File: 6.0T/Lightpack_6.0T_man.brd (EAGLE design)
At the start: 78 x 78.1 mm, 31 parts, among them CN1 USB-MICRO-B-EVT, CN2 RJ11-5P-REEL-LIGHTPACK6T2, CN3 RJ11-5P-REEL-MAIN, IC1 AT90USB162, IC2 DM631_SOP24, IC3 DM631_SOP24, J1 DCJ0202, X1 16Mhz

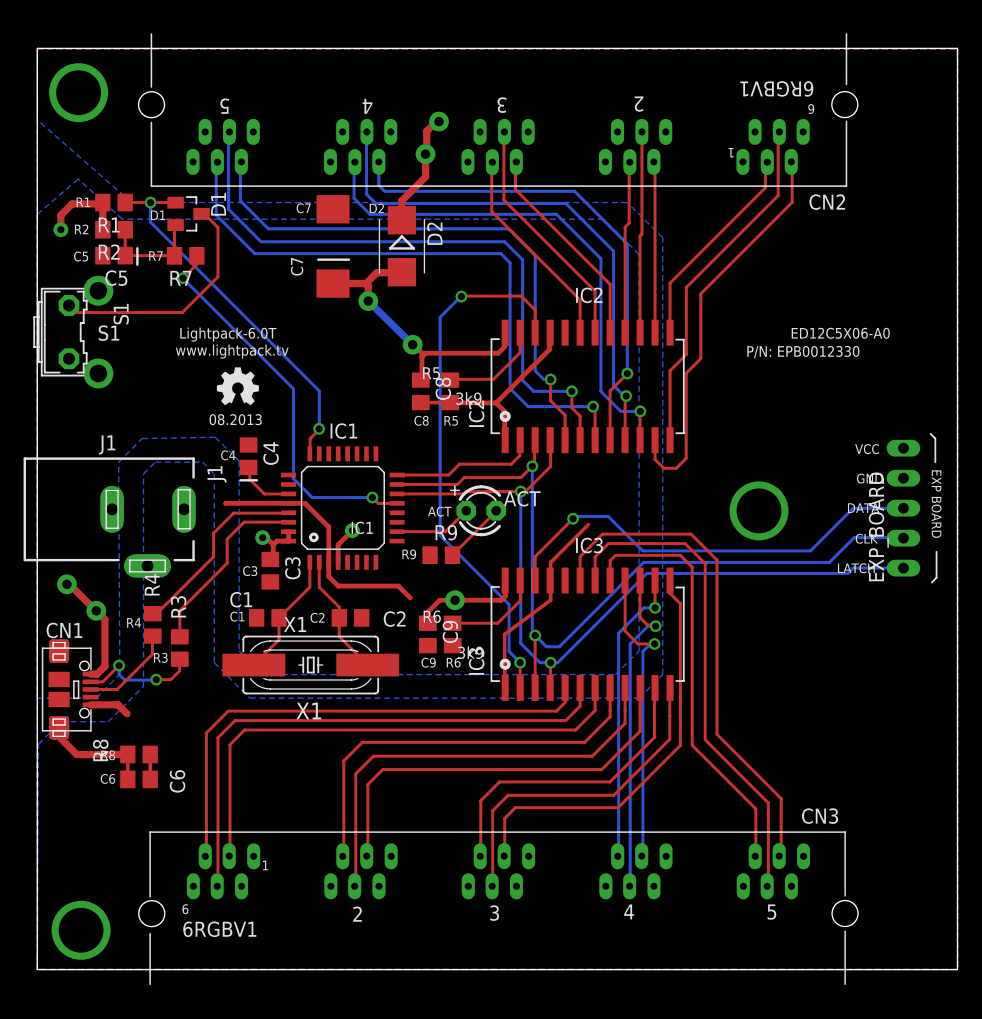
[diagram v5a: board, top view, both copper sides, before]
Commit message: LED, RJ11 reel, Soldermask
— Indicator LED shifted to the exp board on 1.3 mm
— RJ11 reel pads with increased drill diameter
— All vias up to 0.6 diameters now covers with soldermask
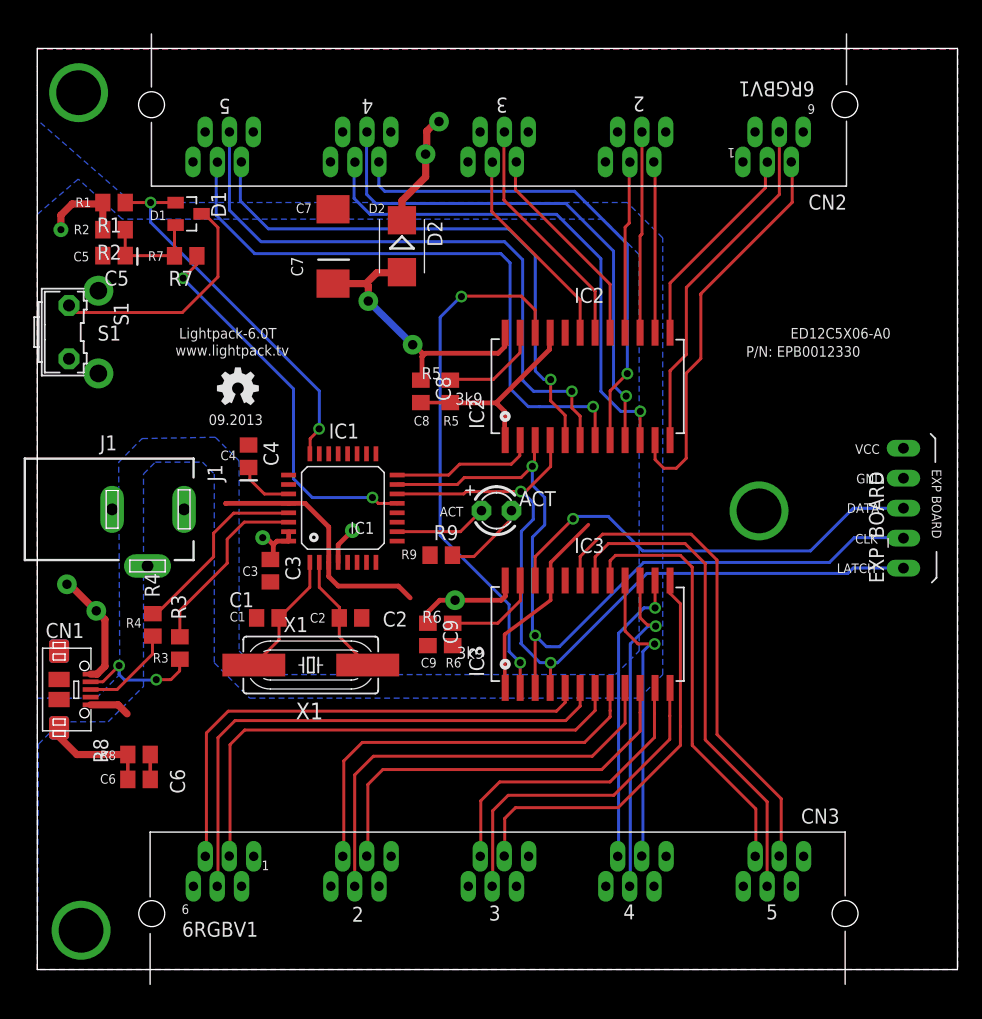
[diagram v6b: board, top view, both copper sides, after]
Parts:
- moved ACT 1.29 mm to (38.9, 40.9)
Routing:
- net N$37: track 5.30 -> 7.08 mm
- net CLK: track 69.7 -> 71.1 mm
- net N$3: track 6.59 -> 7.88 mm
- net LATCH: track 69.3 -> 70.2 mm
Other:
- board text added: "09.2013"
- board text removed: "08.2013"
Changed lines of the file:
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@@
 <?xml version="1.0" encoding="utf-8"?>
 <!DOCTYPE eagle SYSTEM "eagle.dtd">
-<eagle version="6.2">
+<eagle version="6.5.0">
 <drawing>
 <settings>
@@
 <text x="28.07" y="66.09" size="0.8128" layer="21" font="vector">D2</text>
 <text x="9.38" y="62.06" size="0.8128" layer="21" font="vector">R7</text>
-<text x="33.1" y="40.4" size="0.8128" layer="21" font="vector">ACT</text>
+<text x="34.1" y="40.4" size="0.8128" layer="21" font="vector">ACT</text>
 <text x="31.9" y="48.1" size="0.8128" layer="21" font="vector">C8</text>
 <text x="34.4" y="48.1" size="0.8128" layer="21" font="vector">R5</text>
@@
 <rectangle x1="16.7651" y1="53.0274" x2="17.231" y2="53.0309" layer="21"/>
 <rectangle x1="17.2345" y1="53.0274" x2="17.2381" y2="53.0309" layer="21"/>
-<text x="14.52" y="48.15" size="0.9" layer="21" font="vector">08.2013</text>
+<text x="14.52" y="48.15" size="0.9" layer="21" font="vector">09.2013</text>
 <polygon width="0.254" layer="41">
 <vertex x="22.3" y="37.8"/>
@@
 </class>
 </classes>
-<designrules>
+<designrules name="default *">
 <description language="de">&lt;b&gt;EAGLE Design Rules&lt;/b&gt;
 &lt;p&gt;
@@
 <param name="mlMinCreamFrame" value="0mil"/>
 <param name="mlMaxCreamFrame" value="0mil"/>
-<param name="mlViaStopLimit" value="0mil"/>
+<param name="mlViaStopLimit" value="0.6mm"/>
 <param name="srRoundness" value="0"/>
 <param name="srMinRoundness" value="0mil"/>
@@
 <element name="C9" library="rcl" package="C0805" value="100nF" x="33.1" y="30.4" rot="R270"/>
 <element name="D2" library="diode" package="SMB" value="SS14" x="30.9" y="63.3" rot="R270"/>
-<element name="ACT" library="adafruit" package="LED3MM" value="GREEN" x="37.62" y="40.88"/>
+<element name="ACT" library="adafruit" package="LED3MM" value="GREEN" x="38.91" y="40.89"/>
 <element name="R9" library="rcl" package="R0805" value="249R" x="34.23" y="37.12"/>
 <element name="C3" library="rcl" package="C0805" value="100nF" x="19.75" y="35.8" rot="R270"/>
@@
 <wire x1="40.99" y1="43.69" x2="41.95" y2="44.65" width="0.254" layer="1"/>
 <wire x1="42.13" y1="44.83" x2="41.95" y2="44.65" width="0.254" layer="1"/>
-<wire x1="41.95" y1="44.65" x2="41.95" y2="30.55" width="0.254" layer="16"/>
 <wire x1="41.95" y1="30.55" x2="42.19" y2="30.31" width="0.254" layer="16"/>
 <wire x1="42.19" y1="30.31" x2="42.19" y2="30.28" width="0.254" layer="16"/>
@@
 <wire x1="43.38" y1="29.36" x2="43.38" y2="29.38" width="0.254" layer="16"/>
 <wire x1="73.38" y1="38.58" x2="73.4" y2="38.56" width="0.254" layer="16"/>
-<wire x1="73.36" y1="38.6" x2="73.4" y2="38.56" width="0.254" layer="16"/>
 <wire x1="43.14" y1="29.36" x2="44.24" y2="29.36" width="0.254" layer="16"/>
 <wire x1="44.24" y1="29.36" x2="51.38" y2="36.5" width="0.254" layer="16"/>
@@
 <wire x1="69.23" y1="38.6" x2="73.36" y2="38.6" width="0.254" layer="16"/>
 <wire x1="73.36" y1="38.6" x2="73.4" y2="38.56" width="0.254" layer="16"/>
+<wire x1="41.95" y1="44.65" x2="41.95" y2="43.05" width="0.254" layer="16"/>
+<wire x1="41.95" y1="43.05" x2="43" y2="42" width="0.254" layer="16"/>
+<wire x1="42" y1="30.5" x2="42.19" y2="30.31" width="0.254" layer="16"/>
+<wire x1="43" y1="42" x2="43" y2="39.68" width="0.254" layer="16"/>
+<wire x1="43" y1="39.68" x2="41.96" y2="38.64" width="0.254" layer="16"/>
+<wire x1="41.96" y1="38.64" x2="41.96" y2="30.54" width="0.254" layer="16"/>
+<wire x1="41.96" y1="30.54" x2="42.19" y2="30.31" width="0.254" layer="16"/>
 <wire x1="43.14" y1="29.36" x2="43.38" y2="29.36" width="0" layer="19" extent="16-16"/>
 </signal>
@@
 <wire x1="43.5" y1="44.63" x2="43.5" y2="46.825" width="0.254" layer="1"/>
 <wire x1="43.5" y1="46.825" x2="43.46" y2="46.865" width="0.254" layer="1"/>
-<wire x1="40.97" y1="42.51" x2="40.97" y2="29.64" width="0.254" layer="16"/>
 <wire x1="40.97" y1="29.64" x2="42.6" y2="28.01" width="0.254" layer="16"/>
 <wire x1="43.5" y1="28" x2="44.09" y2="28" width="0.254" layer="16"/>
@@
 <wire x1="69.14" y1="36.03" x2="73.39" y2="36.03" width="0.254" layer="16"/>
 <wire x1="73.39" y1="36.03" x2="73.4" y2="36.02" width="0.254" layer="16"/>
+<wire x1="40.97" y1="42.51" x2="41.08" y2="42.51" width="0.254" layer="16"/>
+<wire x1="41.08" y1="42.51" x2="42.03" y2="41.56" width="0.254" layer="16"/>
+<wire x1="42.03" y1="41.56" x2="42.03" y2="40.15" width="0.254" layer="16"/>
+<wire x1="42.03" y1="40.15" x2="41.02" y2="39.14" width="0.254" layer="16"/>
+<wire x1="41.02" y1="39.14" x2="41.02" y2="29.69" width="0.254" layer="16"/>
+<wire x1="41.02" y1="29.69" x2="40.97" y2="29.64" width="0.254" layer="16"/>
 </signal>
 <signal name="DATA3">
@@
 <via x="45.3" y="51" extent="1-16" drill="0.6"/>
 <contactref element="CN2" pad="G5"/>
-<wire x1="45.3" y1="51" x2="42.85" y2="51" width="0.254" layer="16"/>
-<wire x1="16.2" y1="68.5" x2="16.2" y2="72.78" width="0.254" layer="16"/>
-<wire x1="16.2" y1="72.78" x2="16.284" y2="72.984" width="0.254" layer="16"/>
-<wire x1="42.85" y1="51" x2="42.06" y2="51" width="0.254" layer="16"/>
+<wire x1="45.3" y1="51" x2="42.06" y2="51" width="0.254" layer="16"/>
 <wire x1="42.06" y1="51" x2="41.13" y2="51.93" width="0.254" layer="16"/>
 <wire x1="41.13" y1="51.93" x2="41.13" y2="62.15" width="0.254" layer="16"/>
 <wire x1="41.13" y1="62.15" x2="39.6" y2="63.68" width="0.254" layer="16"/>
 <wire x1="39.6" y1="63.68" x2="18.96" y2="63.68" width="0.254" layer="16"/>
-<wire x1="18.96" y1="63.68" x2="16.21" y2="66.43" width="0.254" layer="16"/>
-<wire x1="16.21" y1="66.43" x2="16.21" y2="68.49" width="0.254" layer="16"/>
-<wire x1="16.21" y1="68.49" x2="16.2" y2="68.5" width="0.254" layer="16"/>
+<wire x1="16.284" y1="72.984" x2="16.284" y2="66.356" width="0.254" layer="16"/>
+<wire x1="16.284" y1="66.356" x2="18.96" y2="63.68" width="0.254" layer="16"/>
 </signal>
 <signal name="N$7">
@@
 <wire x1="53.62" y1="52.74" x2="55" y2="54.12" width="0.254" layer="1"/>
 <wire x1="55" y1="54.12" x2="55" y2="59.8" width="0.254" layer="1"/>
-<wire x1="55" y1="59.8" x2="62.78" y2="67.58" width="0.254" layer="1"/>
-<wire x1="62.78" y1="67.58" x2="62.78" y2="72.76" width="0.254" layer="1"/>
-<wire x1="62.78" y1="72.76" x2="62.884" y2="72.984" width="0.254" layer="1"/>
+<wire x1="55" y1="59.8" x2="62.884" y2="67.684" width="0.254" layer="1"/>
+<wire x1="62.884" y1="72.984" x2="62.884" y2="67.684" width="0.254" layer="1"/>
 </signal>
 <signal name="N$15">
@@
 <signal name="N$21">
 <contactref element="IC3" pad="9"/>
-<wire x1="49.81" y1="23.91" x2="49.81" y2="25.865" width="0.254" layer="1"/>
+<wire x1="49.81" y1="22.86" x2="49.81" y2="25.865" width="0.254" layer="1"/>
 <contactref element="CN3" pad="G2"/>
-<wire x1="49.81" y1="23.91" x2="49.81" y2="22.86" width="0.254" layer="1"/>
 <wire x1="49.81" y1="22.86" x2="47.03" y2="20.08" width="0.254" layer="1"/>
 <wire x1="47.03" y1="20.08" x2="28.48" y2="20.08" width="0.254" layer="1"/>
-<wire x1="28.48" y1="20.08" x2="26.99" y2="18.59" width="0.254" layer="1"/>
-<wire x1="26.99" y1="18.59" x2="26.99" y2="9.26" width="0.254" layer="1"/>
-<wire x1="26.99" y1="9.26" x2="26.896" y2="9.056" width="0.254" layer="1"/>
+<wire x1="28.48" y1="20.08" x2="26.896" y2="18.496" width="0.254" layer="1"/>
+<wire x1="26.896" y1="9.056" x2="26.896" y2="18.496" width="0.254" layer="1"/>
 </signal>
 <signal name="N$22">
@@
 <contactref element="CN3" pad="G5"/>
 <wire x1="56.6" y1="36.4" x2="56.6" y2="21.47" width="0.254" layer="1"/>
-<wire x1="56.6" y1="21.47" x2="61.95" y2="16.12" width="0.254" layer="1"/>
-<wire x1="61.95" y1="16.12" x2="61.95" y2="9.27" width="0.254" layer="1"/>
-<wire x1="61.95" y1="9.27" x2="61.846" y2="9.056" width="0.254" layer="1"/>
+<wire x1="61.846" y1="9.056" x2="61.846" y2="16.224" width="0.254" layer="1"/>
+<wire x1="61.846" y1="16.224" x2="56.6" y2="21.47" width="0.254" layer="1"/>
 </signal>
 <signal name="N$43">
@@
 <contactref element="R9" pad="2"/>
 <contactref element="ACT" pad="K"/>
-<wire x1="38.89" y1="40.88" x2="38.89" y2="40.83" width="0.254" layer="1"/>
-<wire x1="38.89" y1="40.83" x2="35.18" y2="37.12" width="0.254" layer="1"/>
+<wire x1="40.18" y1="40.89" x2="40.18" y2="40.18" width="0.254" layer="1"/>
+<wire x1="40.18" y1="40.18" x2="37" y2="37" width="0.254" layer="1"/>
+<wire x1="37" y1="37" x2="35.3" y2="37" width="0.254" layer="1"/>
+<wire x1="35.3" y1="37" x2="35.18" y2="37.12" width="0.254" layer="1"/>
 </signal>
 <signal name="N$14">
@@
 <contactref element="ACT" pad="A"/>
 <contactref element="IC1" pad="10"/>
-<wire x1="30.495" y1="39.1075" x2="34.5775" y2="39.1075" width="0.254" layer="1"/>
-<wire x1="34.5775" y1="39.1075" x2="36.35" y2="40.88" width="0.254" layer="1"/>
+<wire x1="30.495" y1="39.1075" x2="35.8575" y2="39.1075" width="0.254" layer="1"/>
+<wire x1="35.8575" y1="39.1075" x2="37.64" y2="40.89" width="0.254" layer="1"/>
 </signal>
 </signals>
